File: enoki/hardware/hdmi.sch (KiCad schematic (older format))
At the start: 10 parts

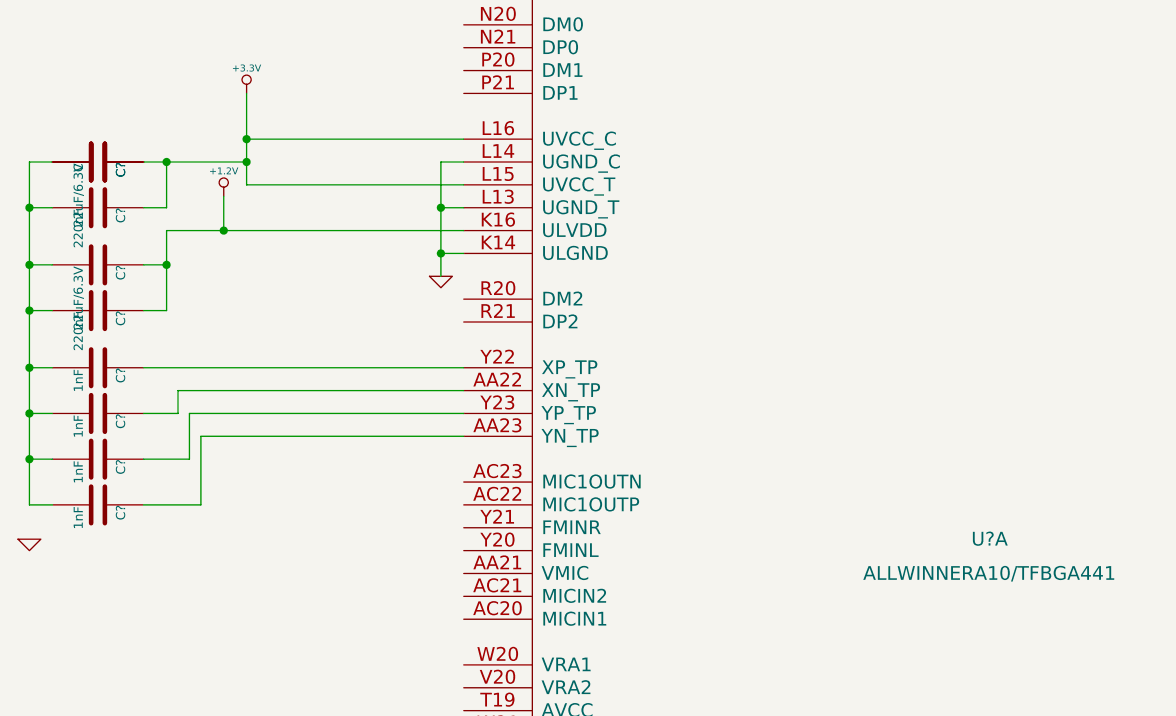
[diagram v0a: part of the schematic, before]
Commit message: ethernet lib added
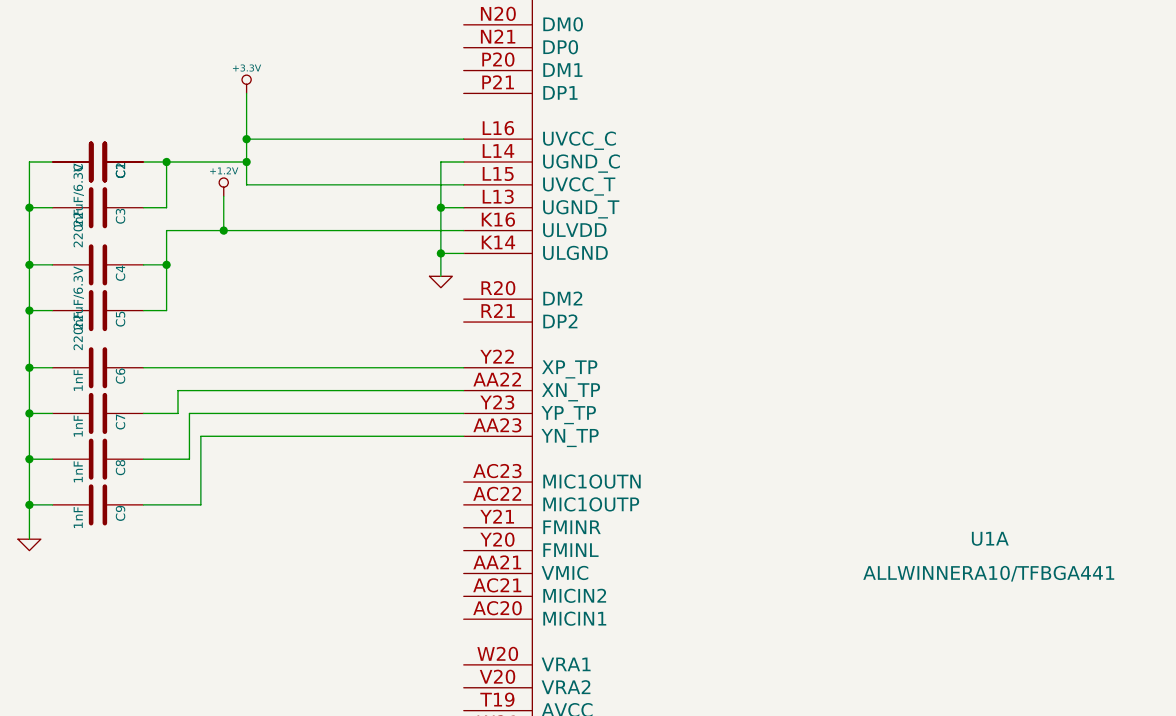
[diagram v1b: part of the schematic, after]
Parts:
- gave numbers to parts that had none: 10
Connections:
- net GND: now also C1.2, C2.2, C3.2, C4.2, C5.2, C6.2, C7.2, C8.2, C9.2
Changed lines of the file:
@@
 $EndDescr
 $Comp
-L ALLWINNERA10/TFBGA441 U?
+L ALLWINNERA10/TFBGA441 U1
 U 1 1 54FD70E1
 P 5500 4000
-F 0 "U?" H 5500 4000 60  0000 C CNN
+F 0 "U1" H 5500 4000 60  0000 C CNN
 F 1 "ALLWINNERA10/TFBGA441" H 5500 3850 60  0000 C CNN
 F 2 "" H 5500 4000 60  0000 C CNN
@@
 $EndComp
 $Comp
-L +3.3V #PWR?
+L +3.3V #PWR01
 U 1 1 54FD7246
 P 2250 2050
-F 0 "#PWR?" H 2250 2010 30  0001 C CNN
+F 0 "#PWR01" H 2250 2010 30  0001 C CNN
 F 1 "+3.3V" H 2250 2160 30  0000 C CNN
 F 2 "" H 2250 2050 60  0000 C CNN
@@
 $EndComp
 $Comp
-L C C?
+L C C1
 U 1 1 54FD7256
 P 1600 2350
-F 0 "C?" H 1600 2450 40  0000 L CNN
+F 0 "C1" H 1600 2450 40  0000 L CNN
 F 1 "22uF/6.3V" H 1606 2265 40  0000 L CNN
 F 2 "~" H 1638 2200 30  0000 C CNN
@@
 $EndComp
 $Comp
-L C C?
+L C C3
 U 1 1 54FD7265
 P 1600 2550
-F 0 "C?" H 1600 2650 40  0000 L CNN
+F 0 "C3" H 1600 2650 40  0000 L CNN
 F 1 "220nF" H 1606 2465 40  0000 L CNN
 F 2 "~" H 1638 2400 30  0000 C CNN
@@
 $EndComp
 $Comp
-L C C?
+L C C2
 U 1 1 54FD728A
 P 1600 2350
-F 0 "C?" H 1600 2450 40  0000 L CNN
+F 0 "C2" H 1600 2450 40  0000 L CNN
 F 1 "C" H 1606 2265 40  0000 L CNN
 F 2 "~" H 1638 2200 30  0000 C CNN
@@
 $EndComp
 $Comp
-L GND #PWR?
+L GND #PWR02
 U 1 1 54FD72D2
 P 3100 2850
-F 0 "#PWR?" H 3100 2850 30  0001 C CNN
+F 0 "#PWR02" H 3100 2850 30  0001 C CNN
 F 1 "GND" H 3100 2780 30  0001 C CNN
 F 2 "" H 3100 2850 60  0000 C CNN
@@
 $EndComp
 $Comp
-L +1.2V #PWR?
+L +1.2V #PWR03
 U 1 1 54FD72F3
 P 2150 2500
-F 0 "#PWR?" H 2150 2640 20  0001 C CNN
+F 0 "#PWR03" H 2150 2640 20  0001 C CNN
 F 1 "+1.2V" H 2150 2610 30  0000 C CNN
 F 2 "" H 2150 2500 60  0000 C CNN
@@
 $EndComp
 $Comp
-L C C?
+L C C5
 U 1 1 54FD733E
 P 1600 3000
-F 0 "C?" H 1600 3100 40  0000 L CNN
+F 0 "C5" H 1600 3100 40  0000 L CNN
 F 1 "220nF" H 1606 2915 40  0000 L CNN
 F 2 "~" H 1638 2850 30  0000 C CNN
@@
 $EndComp
 $Comp
-L C C?
+L C C4
 U 1 1 54FD7344
 P 1600 2800
-F 0 "C?" H 1600 2900 40  0000 L CNN
+F 0 "C4" H 1600 2900 40  0000 L CNN
 F 1 "22uF/6.3V" H 1606 2715 40  0000 L CNN
 F 2 "~" H 1638 2650 30  0000 C CNN
@@
 $EndComp
 $Comp
-L C C?
+L C C6
 U 1 1 54FD73E1
 P 1600 3250
-F 0 "C?" H 1600 3350 40  0000 L CNN
+F 0 "C6" H 1600 3350 40  0000 L CNN
 F 1 "1nF" H 1606 3165 40  0000 L CNN
 F 2 "~" H 1638 3100 30  0000 C CNN
@@
 $EndComp
 $Comp
-L C C?
+L C C7
 U 1 1 54FD7410
 P 1600 3450
-F 0 "C?" H 1600 3550 40  0000 L CNN
+F 0 "C7" H 1600 3550 40  0000 L CNN
 F 1 "1nF" H 1606 3365 40  0000 L CNN
 F 2 "~" H 1638 3300 30  0000 C CNN
@@
 $EndComp
 $Comp
-L C C?
+L C C8
 U 1 1 54FD7416
 P 1600 3650
-F 0 "C?" H 1600 3750 40  0000 L CNN
+F 0 "C8" H 1600 3750 40  0000 L CNN
 F 1 "1nF" H 1606 3565 40  0000 L CNN
 F 2 "~" H 1638 3500 30  0000 C CNN
@@
 $EndComp
 $Comp
-L C C?
+L C C9
 U 1 1 54FD741C
 P 1600 3850
-F 0 "C?" H 1600 3950 40  0000 L CNN
+F 0 "C9" H 1600 3950 40  0000 L CNN
 F 1 "1nF" H 1606 3765 40  0000 L CNN
 F 2 "~" H 1638 3700 30  0000 C CNN
@@
 $EndComp
 $Comp
-L GND #PWR?
+L GND #PWR04
 U 1 1 54FD7587
 P 1300 4000
-F 0 "#PWR?" H 1300 4000 30  0001 C CNN
+F 0 "#PWR04" H 1300 4000 30  0001 C CNN
 F 1 "GND" H 1300 3930 30  0001 C CNN
 F 2 "" H 1300 4000 60  0000 C CNN
@@
 	1400 2350 1300 2350
 Wire Wire Line
-	1300 2350 1300 3850
+	1300 2350 1300 4000
 Wire Wire Line
 	1300 2550 1400 2550
@@
 Wire Wire Line
 	2050 3850 1800 3850
+Connection ~ 1300 3850
 $EndSCHEMATC

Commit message: initual commit
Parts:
- removed C1, C4: 22uF/6.3V, ~, symbol C
- removed C2: C, ~, symbol C
- removed C3, C5: 220nF, ~, symbol C
- removed C6, C7, C8, C9: 1nF, ~, symbol C
- removed U1: ALLWINNERA10/TFBGA441, symbol ALLWINNERA10/TFBGA441
